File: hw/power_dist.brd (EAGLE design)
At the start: 80 x 50 mm, 78 parts, among them J1 JST-ZH6SMT_VERT, J2 JST-PH4SMT_VERT, J3 JST-PH5VERT, P1 XT30P, P2 XT30P, P3 XT30P, P4 XT30P, P5 XT30P, P6 XT30P, P7 XT90PW-M, Q1 PSMN4R8-100BSEJ, Q2 PSMN4R8-100BSEJ, Q3 PSMN4R8-100BSEJ, Q4 MF-DSC-SOT233-MMBT3904, Q5 MMBT5401 100V, U1 MAX15062AATA+T, U2 STM32G474CEU6, U4 TCAN334G, U5 LT1787HVIMS8PBF, U6 LTC4830

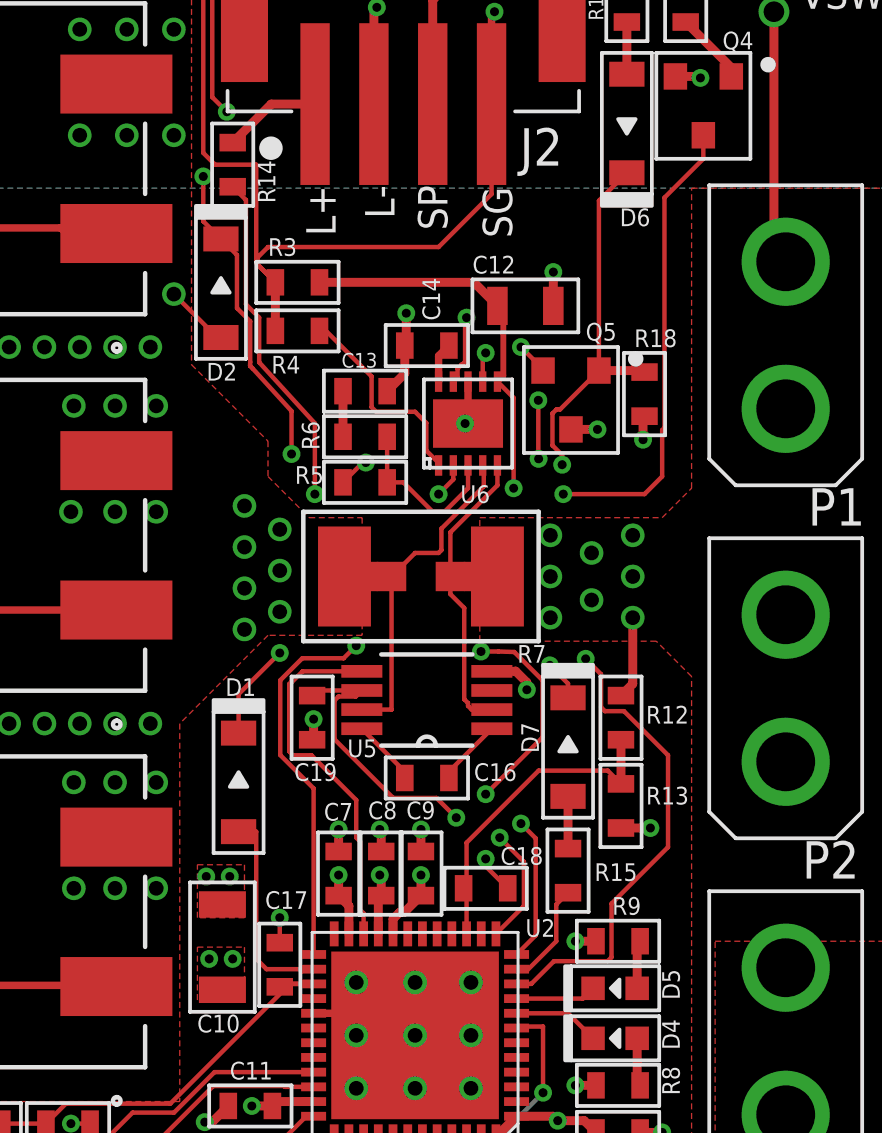
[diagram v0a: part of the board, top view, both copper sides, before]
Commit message: Add more debugging pads
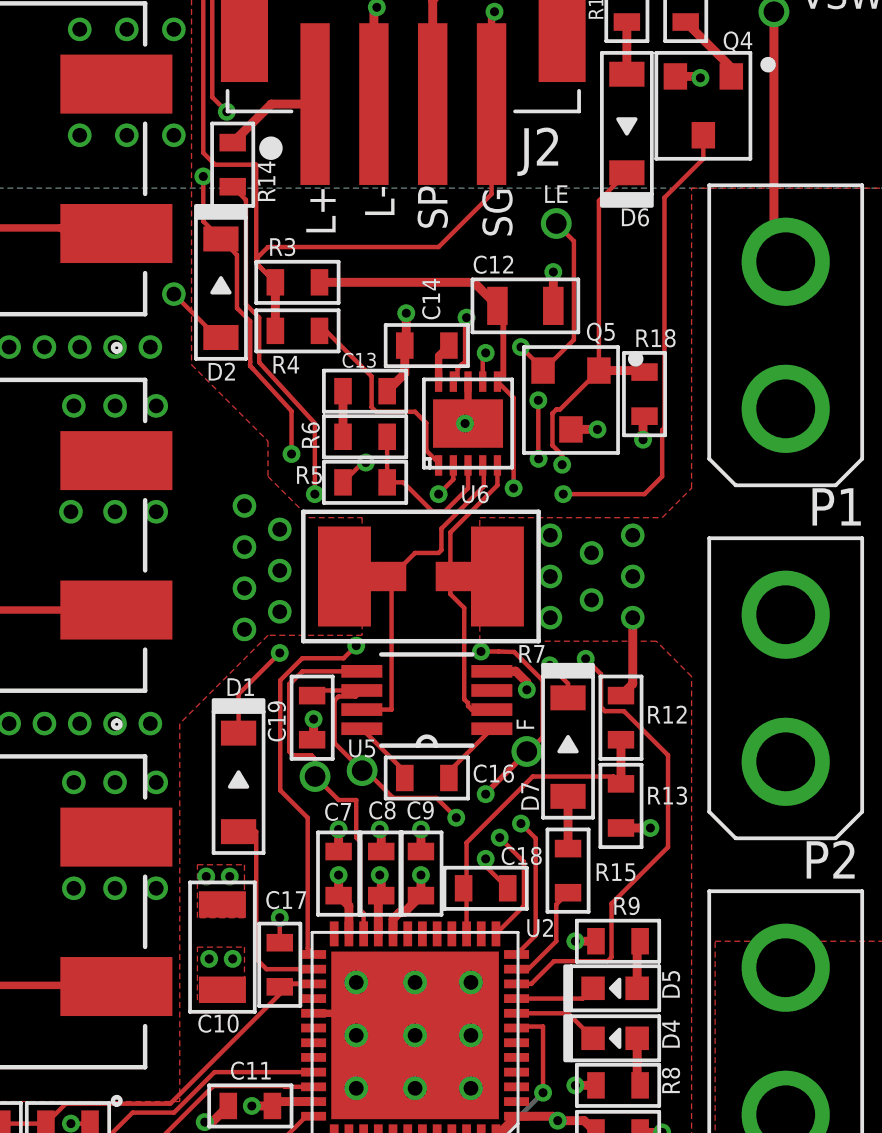
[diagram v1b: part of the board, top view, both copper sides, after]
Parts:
- added DB_FLT, DB_IB, DB_IS, DB_LEN: PAD24AWG_PAD, precharge:24AWG_PAD
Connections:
- net FLT: now also DB_FLT.P$1
- net ISAMP: now also DB_IS.P$1
- net ISAMP_BIAS: now also DB_IB.P$1
- net LTC_EN: now also DB_LEN.P$1
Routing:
- net LTC_EN: track 5.75 -> 11.4 mm
- net FLT: track 26.1 -> 28.2 mm
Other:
- board text added: "F"
- board text added: "LE"
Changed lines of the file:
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@@
 <text x="21.9" y="48.7" size="1" layer="21">VIN</text>
 <text x="68.5" y="48.1" size="1" layer="21">VSW</text>
+<text x="59.45" y="23.55" size="0.6" layer="25" font="vector" ratio="10" rot="R90">F</text>
+<text x="59.75" y="41.5" size="0.6" layer="25" font="vector" ratio="10">LE</text>
 </plain>
 <attributes>
@@
 <attribute name="HOUSEPART" value="" x="55.8" y="21.95" size="1.778" layer="27" rot="R180" display="off"/>
 <attribute name="MPN" value="" x="55.8" y="21.95" size="1.778" layer="27" rot="R180" display="off"/>
-<attribute name="NAME" x="57.4" y="21.85" size="0.6" layer="25" font="vector" ratio="10"/>
+<attribute name="NAME" x="57.35" y="21.8" size="0.6" layer="25" font="vector" ratio="10"/>
 <attribute name="POPULATE" value="0" x="55.8" y="21.95" size="1.778" layer="27" rot="R180" display="off"/>
 <attribute name="TOLERANCE" value="" x="55.8" y="21.95" size="1.778" layer="27" rot="R180" display="off"/>
@@
 <attribute name="HOUSEPART" value="1" x="51.9" y="24" size="1.778" layer="27" rot="R270" display="off"/>
 <attribute name="MPN" value="MF-CAP-0603-0.1uF" x="51.9" y="24" size="1.778" layer="27" rot="R270" display="off"/>
-<attribute name="NAME" x="52.75" y="22.45" size="0.6" layer="25" font="vector" ratio="10" rot="R180"/>
+<attribute name="NAME" x="51" y="23.15" size="0.6" layer="25" font="vector" ratio="10" rot="R90"/>
 <attribute name="POPULATE" value="1" x="51.9" y="24" size="1.778" layer="27" rot="R270" display="off"/>
 <attribute name="TOLERANCE" value="" x="51.9" y="24" size="1.778" layer="27" rot="R270" display="off"/>
@@
 <attribute name="HOUSEPART" value="YES" x="60.6" y="23" size="1.778" layer="27" rot="R270" display="off"/>
 <attribute name="MPN" value="MF-DIO-SOD123-1N4148" x="60.6" y="23" size="1.778" layer="27" rot="R270" display="off"/>
-<attribute name="NAME" x="59.61" y="22.8" size="0.6" layer="25" font="vector" ratio="10" rot="R90"/>
+<attribute name="NAME" x="59.61" y="20.8" size="0.6" layer="25" font="vector" ratio="10" rot="R90"/>
 <attribute name="POPULATE" value="1" x="60.6" y="23" size="1.778" layer="27" rot="R270" display="off"/>
 <attribute name="URL" value="https://factory.macrofab.com/part/MF-DIO-SOD123-1N4148" x="60.6" y="23" size="1.778" layer="27" rot="R270" display="off"/>
@@
 <attribute name="URL" value="" x="50.8" y="15.6" size="1.778" layer="27" rot="R90" display="off"/>
 <attribute name="VOLTAGE" value="" x="50.8" y="15.6" size="1.778" layer="27" rot="R90" display="off"/>
+</element>
+<element name="DB_LEN" library="precharge" package="24AWG_PAD" value="PAD24AWG_PAD" x="60.2" y="40.8" smashed="yes">
+<attribute name="POPULATE" value="0" x="60.2" y="40.8" size="1.778" layer="27" display="off"/>
+</element>
+<element name="DB_FLT" library="precharge" package="24AWG_PAD" value="PAD24AWG_PAD" x="59.2" y="22.85" smashed="yes">
+<attribute name="POPULATE" value="0" x="59.2" y="22.85" size="1.778" layer="27" display="off"/>
+</element>
+<element name="DB_IB" library="precharge" package="24AWG_PAD" value="PAD24AWG_PAD" x="53.6" y="22.2" smashed="yes">
+<attribute name="POPULATE" value="0" x="53.6" y="22.2" size="0.6" layer="27" font="vector" ratio="10" display="off"/>
+</element>
+<element name="DB_IS" library="precharge" package="24AWG_PAD" value="PAD24AWG_PAD" x="52" y="22" smashed="yes">
+<attribute name="POPULATE" value="0" x="52" y="22" size="0.6" layer="27" font="vector" ratio="10" display="off"/>
 </element>
 </elements>
@@
 <via x="53.4" y="26.4481" extent="1-16" drill="0.3048"/>
 <wire x1="53.4" y1="26.4481" x2="52.9714" y2="26.0195" width="0.1524" layer="1"/>
-<wire x1="50.8166" y1="25.27094375" x2="50.8166" y2="22.72905625" width="0.1524" layer="1"/>
-<wire x1="51.95" y1="21.59565625" x2="51.95" y2="15.95" width="0.1524" layer="1"/>
-<wire x1="50.8166" y1="22.72905625" x2="51.95" y2="21.59565625" width="0.1524" layer="1"/>
+<wire x1="50.8166" y1="25.27094375" x2="50.8166" y2="21.52905625" width="0.1524" layer="1"/>
+<wire x1="51.75" y1="20.59565625" x2="51.75" y2="16.15" width="0.1524" layer="1"/>
+<wire x1="51.75" y1="16.15" x2="51.95" y2="15.95" width="0.1524" layer="1"/>
+<wire x1="50.8166" y1="21.52905625" x2="51.75" y2="20.59565625" width="0.1524" layer="1"/>
 <wire x1="52.9714" y1="26.0195" x2="51.56515625" y2="26.0195" width="0.1524" layer="1"/>
 <wire x1="51.56515625" y1="26.0195" x2="50.8166" y2="25.27094375" width="0.1524" layer="1"/>
@@
 <wire x1="59.1" y1="17.6" x2="58.15" y2="16.65" width="0.1524" layer="1"/>
 <wire x1="57.8" y1="21.4" x2="57.8" y2="20.4" width="0.1524" layer="2"/>
+<contactref element="DB_FLT" pad="P$1"/>
+<wire x1="57.8" y1="21.4" x2="57.8" y2="21.45" width="0.1524" layer="1"/>
+<wire x1="57.8" y1="21.45" x2="59.2" y2="22.85" width="0.1524" layer="1"/>
 </signal>
 <signal name="ISAMP_BIAS">
@@
 <wire x1="51.9" y1="24.75" x2="52.075" y2="24.925" width="0.1524" layer="1"/>
 <wire x1="52.075" y1="24.925" x2="53.5902" y2="24.925" width="0.1524" layer="1"/>
-<wire x1="52.7970125" y1="24.7195" x2="52.6631" y2="24.5855875" width="0.1524" layer="1"/>
-<wire x1="53.5902" y1="24.925" x2="53.3847" y2="24.7195" width="0.1524" layer="1"/>
-<wire x1="53.3847" y1="24.7195" x2="52.7970125" y2="24.7195" width="0.1524" layer="1"/>
 <wire x1="56.1286" y1="21.2714" x2="56.8" y2="20.6" width="0.1524" layer="1"/>
 <wire x1="54.6553125" y1="21.2714" x2="56.1286" y2="21.2714" width="0.1524" layer="1"/>
-<wire x1="52.6631" y1="24.5855875" x2="52.6631" y2="23.2636125" width="0.1524" layer="1"/>
-<wire x1="52.6631" y1="23.2636125" x2="54.6553125" y2="21.2714" width="0.1524" layer="1"/>
+<wire x1="52.6631" y1="24.5855875" x2="52.6631" y2="23.1369" width="0.1524" layer="1"/>
 <via x="56.8" y="20.6" extent="1-16" drill="0.3048"/>
 <wire x1="56.8" y1="20.6" x2="59" y2="20.6" width="0.1524" layer="15"/>
@@
 <wire x1="59.5" y1="19.9" x2="59.5" y2="16.6" width="0.1524" layer="1"/>
 <wire x1="59.5" y1="16.6" x2="58.85" y2="15.95" width="0.1524" layer="1"/>
+<contactref element="DB_IB" pad="P$1"/>
+<wire x1="52.6631" y1="24.5855875" x2="52.7970125" y2="24.7195" width="0.1524" layer="1"/>
+<wire x1="52.7970125" y1="24.7195" x2="53.3847" y2="24.7195" width="0.1524" layer="1"/>
+<wire x1="53.3847" y1="24.7195" x2="53.5902" y2="24.925" width="0.1524" layer="1"/>
+<wire x1="53.6" y1="22.2" x2="52.6631" y2="23.1369" width="0.1524" layer="1"/>
+<wire x1="53.6" y1="22.2" x2="53.7267125" y2="22.2" width="0.1524" layer="1"/>
+<wire x1="53.7267125" y1="22.2" x2="54.6553125" y2="21.2714" width="0.1524" layer="1"/>
 </signal>
 <signal name="ISAMP">
@@
 <wire x1="51.1214" y1="25.1446875" x2="51.2" y2="25.2232875" width="0.1524" layer="1"/>
 <wire x1="51.2" y1="25.2232875" x2="51.2" y2="25.2" width="0.1524" layer="1"/>
-<wire x1="53.4" y1="21.2" x2="51.8786" y2="22.7214" width="0.1524" layer="1"/>
-<wire x1="51.8786" y1="22.7214" x2="51.2553125" y2="22.7214" width="0.1524" layer="1"/>
+<wire x1="51.2553125" y1="22.7214" x2="51.8786" y2="22.7214" width="0.1524" layer="1"/>
 <wire x1="51.1214" y1="22.8553125" x2="51.1214" y2="25.1446875" width="0.1524" layer="1"/>
 <wire x1="51.2" y1="25.2" x2="51.575" y2="25.575" width="0.1524" layer="1"/>
 <wire x1="51.575" y1="25.575" x2="53.5902" y2="25.575" width="0.1524" layer="1"/>
+<contactref element="DB_IS" pad="P$1"/>
+<wire x1="51.8786" y1="22.7214" x2="52" y2="22.6" width="0.1524" layer="1"/>
+<wire x1="52" y1="22.6" x2="52" y2="22" width="0.1524" layer="1"/>
+<wire x1="53.4" y1="21.2" x2="52.8" y2="21.2" width="0.1524" layer="1"/>
+<wire x1="52.8" y1="21.2" x2="52" y2="22" width="0.1524" layer="1"/>
 </signal>
 <signal name="N$6">
@@
 <wire x1="58" y1="37.6" x2="57.15" y2="37.6" width="0.1524" layer="15"/>
 <wire x1="58" y1="37.6" x2="59" y2="36.6" width="0.1524" layer="15"/>
+<contactref element="DB_LEN" pad="P$1"/>
+<wire x1="60.2" y1="40.8" x2="60.8" y2="40.2" width="0.1524" layer="1"/>
+<wire x1="60.8" y1="36.85" x2="59.75" y2="35.8" width="0.1524" layer="1"/>
+<wire x1="60.8" y1="40.2" x2="60.8" y2="36.85" width="0.1524" layer="1"/>
 </signal>
 <signal name="N$13">
@@
 <contactref element="R12" pad="P$1"/>
 <wire x1="62.4" y1="23.25" x2="62.4" y2="21.75" width="0.3048" layer="1"/>
-<wire x1="62.4" y1="21.75" x2="61.95" y2="22.2" width="0.1524" layer="1"/>
-<wire x1="61.95" y1="22.2" x2="59.6" y2="22.2" width="0.1524" layer="1"/>
-<wire x1="59.6" y1="22.2" x2="57.15" y2="19.75" width="0.1524" layer="1"/>
+<wire x1="62.4" y1="21.75" x2="62.15" y2="22" width="0.1524" layer="1"/>
+<wire x1="62.15" y1="22" x2="59.4" y2="22" width="0.1524" layer="1"/>
+<wire x1="59.4" y1="22" x2="57.15" y2="19.75" width="0.1524" layer="1"/>
 <wire x1="57.15" y1="19.75" x2="57.15" y2="18.2" width="0.1524" layer="1"/>
 <contactref element="C18" pad="P$1"/>

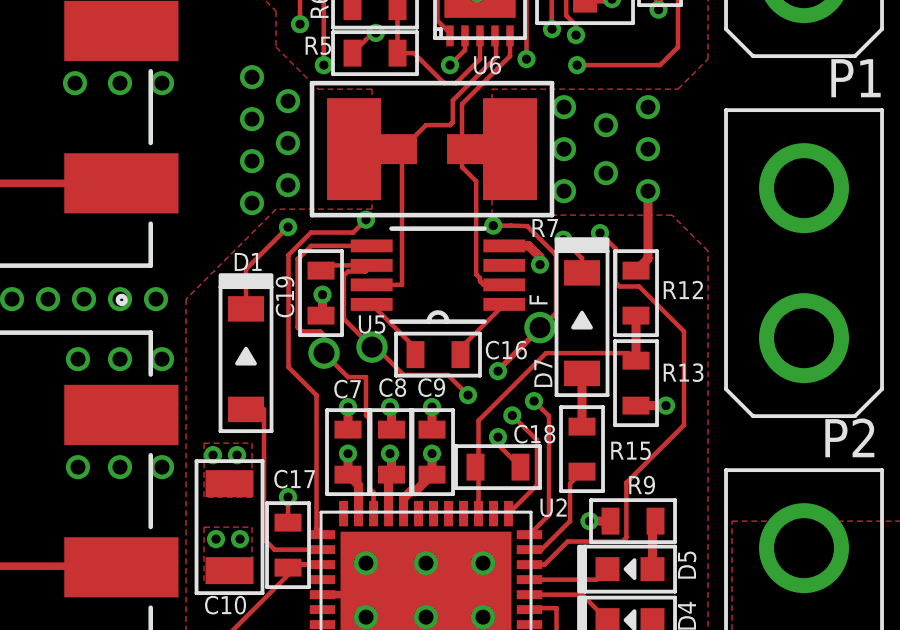
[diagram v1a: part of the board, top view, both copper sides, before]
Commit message: More debug pad position tweaks
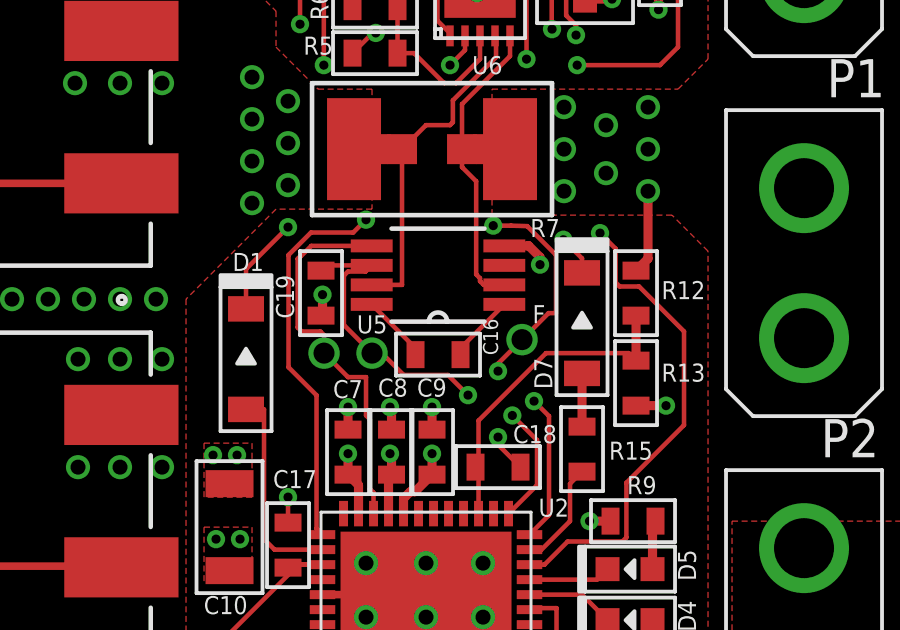
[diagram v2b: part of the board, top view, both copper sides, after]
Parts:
- moved DB_FLT 0.72 mm to (58.6, 22.4)
- moved DB_IB 0.20 mm to (53.6, 22.0)
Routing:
- net FLT: track 28.2 -> 26.3 mm
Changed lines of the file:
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@@
 <text x="21.9" y="48.7" size="1" layer="21">VIN</text>
 <text x="68.5" y="48.1" size="1" layer="21">VSW</text>
-<text x="59.45" y="23.55" size="0.6" layer="25" font="vector" ratio="10" rot="R90">F</text>
+<text x="58.95" y="23" size="0.6" layer="25" font="vector" ratio="10">F</text>
 <text x="59.75" y="41.5" size="0.6" layer="25" font="vector" ratio="10">LE</text>
 </plain>
@@
 <attribute name="HOUSEPART" value="" x="55.8" y="21.95" size="1.778" layer="27" rot="R180" display="off"/>
 <attribute name="MPN" value="" x="55.8" y="21.95" size="1.778" layer="27" rot="R180" display="off"/>
-<attribute name="NAME" x="57.35" y="21.8" size="0.6" layer="25" font="vector" ratio="10"/>
+<attribute name="NAME" x="57.3" y="23.15" size="0.5" layer="25" font="vector" ratio="10" rot="R270"/>
 <attribute name="POPULATE" value="0" x="55.8" y="21.95" size="1.778" layer="27" rot="R180" display="off"/>
 <attribute name="TOLERANCE" value="" x="55.8" y="21.95" size="1.778" layer="27" rot="R180" display="off"/>
@@
 <attribute name="POPULATE" value="0" x="60.2" y="40.8" size="1.778" layer="27" display="off"/>
 </element>
-<element name="DB_FLT" library="precharge" package="24AWG_PAD" value="PAD24AWG_PAD" x="59.2" y="22.85" smashed="yes">
-<attribute name="POPULATE" value="0" x="59.2" y="22.85" size="1.778" layer="27" display="off"/>
-</element>
-<element name="DB_IB" library="precharge" package="24AWG_PAD" value="PAD24AWG_PAD" x="53.6" y="22.2" smashed="yes">
-<attribute name="POPULATE" value="0" x="53.6" y="22.2" size="0.6" layer="27" font="vector" ratio="10" display="off"/>
+<element name="DB_FLT" library="precharge" package="24AWG_PAD" value="PAD24AWG_PAD" x="58.6" y="22.45" smashed="yes">
+<attribute name="POPULATE" value="0" x="58.6" y="22.45" size="1.778" layer="27" display="off"/>
+</element>
+<element name="DB_IB" library="precharge" package="24AWG_PAD" value="PAD24AWG_PAD" x="53.6" y="22" smashed="yes">
+<attribute name="POPULATE" value="0" x="53.6" y="22" size="0.6" layer="27" font="vector" ratio="10" display="off"/>
 </element>
 <element name="DB_IS" library="precharge" package="24AWG_PAD" value="PAD24AWG_PAD" x="52" y="22" smashed="yes">
@@
 <wire x1="58.77094375" y1="26.2334" x2="58.235128125" y2="26.25" width="0.1524" layer="1"/>
 <wire x1="57.6404" y1="26.25" x2="58.235128125" y2="26.25" width="0.1524" layer="1"/>
-<wire x1="59.7334" y1="25.27094375" x2="59.7334" y2="23.3334" width="0.1524" layer="1"/>
-<wire x1="59.7334" y1="23.3334" x2="57.8" y2="21.4" width="0.1524" layer="1"/>
+<wire x1="59.7334" y1="23.3334" x2="59.7334" y2="25.27094375" width="0.1524" layer="1"/>
 <via x="57.8" y="21.4" extent="1-16" drill="0.3048"/>
 <wire x1="57.8" y1="20.4" x2="58.277171875" y2="19.922828125" width="0.1524" layer="2"/>
@@
 <wire x1="57.8" y1="21.4" x2="57.8" y2="20.4" width="0.1524" layer="2"/>
 <contactref element="DB_FLT" pad="P$1"/>
-<wire x1="57.8" y1="21.4" x2="57.8" y2="21.45" width="0.1524" layer="1"/>
-<wire x1="57.8" y1="21.45" x2="59.2" y2="22.85" width="0.1524" layer="1"/>
+<wire x1="57.8" y1="21.4" x2="57.8" y2="21.65" width="0.1524" layer="1"/>
+<wire x1="57.8" y1="21.65" x2="58.6" y2="22.45" width="0.1524" layer="1"/>
+<wire x1="58.6" y1="22.45" x2="59.4834" y2="23.3334" width="0.1524" layer="1"/>
+<wire x1="59.4834" y1="23.3334" x2="59.7334" y2="23.3334" width="0.1524" layer="1"/>
 </signal>
 <signal name="ISAMP_BIAS">
@@
 <wire x1="56.1286" y1="21.2714" x2="56.8" y2="20.6" width="0.1524" layer="1"/>
 <wire x1="54.6553125" y1="21.2714" x2="56.1286" y2="21.2714" width="0.1524" layer="1"/>
-<wire x1="52.6631" y1="24.5855875" x2="52.6631" y2="23.1369" width="0.1524" layer="1"/>
+<wire x1="52.6631" y1="24.5855875" x2="52.6631" y2="22.9369" width="0.1524" layer="1"/>
 <via x="56.8" y="20.6" extent="1-16" drill="0.3048"/>
 <wire x1="56.8" y1="20.6" x2="59" y2="20.6" width="0.1524" layer="15"/>
@@
 <wire x1="52.7970125" y1="24.7195" x2="53.3847" y2="24.7195" width="0.1524" layer="1"/>
 <wire x1="53.3847" y1="24.7195" x2="53.5902" y2="24.925" width="0.1524" layer="1"/>
-<wire x1="53.6" y1="22.2" x2="52.6631" y2="23.1369" width="0.1524" layer="1"/>
-<wire x1="53.6" y1="22.2" x2="53.7267125" y2="22.2" width="0.1524" layer="1"/>
-<wire x1="53.7267125" y1="22.2" x2="54.6553125" y2="21.2714" width="0.1524" layer="1"/>
+<wire x1="53.6" y1="22" x2="52.6631" y2="22.9369" width="0.1524" layer="1"/>
+<wire x1="53.6" y1="22" x2="53.9267125" y2="22" width="0.1524" layer="1"/>
+<wire x1="53.9267125" y1="22" x2="54.6553125" y2="21.2714" width="0.1524" layer="1"/>
 </signal>
 <signal name="ISAMP">
